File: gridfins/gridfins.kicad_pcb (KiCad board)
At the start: 4 copper layers, 76 parts, among them J1 RBUS, J2 USB_C_Receptacle_USB2.0, U1 ESP32-S3, U2 SN65HVD230, U3 LM66200DRLR, U4 MAX77827AEFD+T, U5 SC4215ASTRT, Y1 R940000171

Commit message: Update with Inertial Measurement Unit
cloned IMU from pickle rick.
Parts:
- added C12: 10uF, Capacitor_SMD:C_0402_1005Metric, F.Cu at (174.7, 55.1)
- added C18: 160pF, Capacitor_SMD:C_0603_1608Metric, F.Cu at (165.3, 29.6)
- added C19: 47uF, Capacitor_SMD:C_1206_3216Metric, F.Cu at (150.6, 22.3)
- added C28: 1uF, Capacitor_SMD:C_0402_1005Metric, F.Cu at (168.4, 36.7)
- added C29: 4.7uF, Capacitor_SMD:C_0402_1005Metric, F.Cu at (168.4, 38.7)
- added C30: 100uF, Capacitor_Tantalum_SMD:CP_EIA-7360-38_Kemet-E, F.Cu at (158.4, 24.4)
- added C31: 47uF, Capacitor_SMD:C_1206_3216Metric, F.Cu at (150.6, 25.7)
- added C32: 100uF, Capacitor_Tantalum_SMD:CP_EIA-7360-38_Kemet-E, F.Cu at (158.4, 32.0)
- added C33: 47uF, Capacitor_SMD:C_1206_3216Metric, F.Cu at (150.6, 29.0)
- added C34: 100nF, Capacitor_SMD:C_0402_1005Metric, F.Cu at (174.7, 57.1)
- added C35: 47uF, Capacitor_SMD:C_1206_3216Metric, F.Cu at (150.6, 32.4)
- added C36: 0.47uF, Capacitor_SMD:C_0402_1005Metric, F.Cu at (174.7, 59.0)
- added C37: 47uF, Capacitor_SMD:C_1206_3216Metric, F.Cu at (150.6, 35.7)
- added C38: 100nF, Capacitor_SMD:C_0402_1005Metric, F.Cu at (168.4, 40.7)
- added C39: 0.1uF, Capacitor_SMD:C_0402_1005Metric, F.Cu at (168.4, 42.6)
- added C40: 47uF, Capacitor_SMD:C_1206_3216Metric, F.Cu at (150.6, 39.1)
- added C41: 10nF, Capacitor_SMD:C_0402_1005Metric, F.Cu at (174.7, 61.0)
- added C42: 0.1uF, Capacitor_SMD:C_0402_1005Metric, F.Cu at (174.7, 63.0)
- added C43: 2.2uF, Capacitor_SMD:C_0402_1005Metric, F.Cu at (174.7, 65.0)
- added C44: 10uF, Capacitor_SMD:C_0402_1005Metric, F.Cu at (174.7, 66.9)
- added C45: 0.1uF, Capacitor_SMD:C_0402_1005Metric, F.Cu at (187.8, 57.1)
- added C46: 47uF, Capacitor_SMD:C_1206_3216Metric, F.Cu at (150.6, 42.4)
- added C47: 47uF, Capacitor_SMD:C_1206_3216Metric, F.Cu at (150.6, 45.8)
- added C48: 47uF, Capacitor_SMD:C_1206_3216Metric, F.Cu at (150.6, 49.1)
- added C49: 47uF, Capacitor_SMD:C_1206_3216Metric, F.Cu at (150.6, 52.5)
- added C50: 1uF, Capacitor_SMD:C_0402_1005Metric, F.Cu at (174.7, 68.9)
- added D3: LED, LED_SMD:LED_0402_1005Metric, F.Cu at (188.1, 55.1)
- added D4: ~, Package_TO_SOT_SMD:SOT-353_SC-70-5, F.Cu at (188.9, 22.7)
- added D5: ~, Package_TO_SOT_SMD:SOT-353_SC-70-5, F.Cu at (188.9, 26.6)
- added D6: ~, Package_TO_SOT_SMD:SOT-353_SC-70-5, F.Cu at (188.9, 30.5)
- added D7: ~, Package_TO_SOT_SMD:SOT-353_SC-70-5, F.Cu at (188.9, 34.4)
- added J3: ServoCH0, iclr:Molex_Nano-Fit_105313-xx03_1x03_P2.50mm_Horizontal, F.Cu at (175.4, 23.4)
- added J4: ServoCH1, iclr:Molex_Nano-Fit_105313-xx03_1x03_P2.50mm_Horizontal, F.Cu at (175.4, 33.9)
- added J5: ServoCH2, iclr:Molex_Nano-Fit_105313-xx03_1x03_P2.50mm_Horizontal, F.Cu at (175.4, 44.4)
- added L4: 3.3uH, iclr:IND_SPM10065VT-3R3M-D, F.Cu at (160.2, 41.5)
- added Q1: SSM3K15AMFV,L3F, iclr:SOT-723, F.Cu at (169.1, 29.8)
- added R19: R, Resistor_SMD:R_0402_1005Metric, F.Cu at (184.9, 55.1)
- added R20: 10k, Resistor_SMD:R_0402_1005Metric, F.Cu at (154.8, 48.3)
- added R21: 113k, Resistor_SMD:R_0402_1005Metric, F.Cu at (154.8, 50.3)
- added R22: 200k, Resistor_SMD:R_0402_1005Metric, F.Cu at (154.8, 52.3)
- added R23: 100k, Resistor_SMD:R_0402_1005Metric, F.Cu at (157.8, 48.3)
- added R24: 442k, Resistor_SMD:R_0402_1005Metric, F.Cu at (157.8, 50.3)
- added R25: 165R, Resistor_SMD:R_0402_1005Metric, F.Cu at (188.2, 37.4)
- added R26: 165R, Resistor_SMD:R_0402_1005Metric, F.Cu at (188.2, 39.3)
- added R27: 165R, Resistor_SMD:R_0402_1005Metric, F.Cu at (188.2, 41.3)
- added R28: 10k, Resistor_SMD:R_0402_1005Metric, F.Cu at (157.8, 52.3)
- added R29: 2.2, Resistor_SMD:R_0402_1005Metric, F.Cu at (160.7, 48.3)
- added R34: 18k, Resistor_SMD:R_0402_1005Metric, F.Cu at (184.9, 57.1)
- added R36: 1.5k, Resistor_SMD:R_0402_1005Metric, F.Cu at (184.9, 59.1)
- added R37: 470, Resistor_SMD:R_0402_1005Metric, F.Cu at (184.9, 61.1)
- added R38: 10k, Resistor_SMD:R_0402_1005Metric, F.Cu at (160.7, 50.3)
- added R39: 1k, Resistor_SMD:R_0402_1005Metric, F.Cu at (160.7, 52.3)
- added R42: 5.1R, Resistor_SMD:R_0603_1608Metric, F.Cu at (165.3, 32.1)
- added TP25: TestPoint, TestPoint:TestPoint_Pad_D1.0mm, F.Cu at (108.9, 89.5)
- added TP26: TestPoint, TestPoint:TestPoint_Pad_D1.0mm, F.Cu at (108.9, 92.6)
- added TP27: TestPoint, TestPoint:TestPoint_Pad_D1.0mm, F.Cu at (108.9, 95.6)
- added U6: SiC437AED-T1, iclr:SiC437BEDT1GE3, F.Cu at (167.3, 24.6)
- added U7: ICM-20608-G, iclr:PQFN50P300X300X80-16N, F.Cu at (179.0, 61.8)
- added U8: MMC5983MA, iclr:PQFN50P300X300X100-16N, F.Cu at (178.8, 66.3)
- added U9: H3LIS331DLTR, iclr:QFN300X300X100-16N, F.Cu at (178.8, 56.8)
- moved C11 75.4 mm to (98.5, 41.2)
- moved C13 75.4 mm to (98.5, 43.2)
- moved C14 75.4 mm to (98.5, 45.1)
- moved D1 75.4 mm to (111.6, 73.4)
- moved J1 75.4 mm to (79.2, 45.2)
- moved JP3 75.4 mm to (92.1, 55.9)
- moved L1 75.4 mm to (92.7, 31.3)
- moved L2 75.4 mm to (92.7, 33.2)
- moved R1 75.4 mm to (92.7, 35.2)
- moved R18 75.4 mm to (95.7, 39.2)
- moved R2 75.4 mm to (92.7, 37.2)
- moved R3 75.4 mm to (92.7, 39.2)
- moved R4 75.4 mm to (95.7, 31.3)
- moved R5 75.4 mm to (95.7, 33.2)
- moved R6 75.4 mm to (95.7, 35.2)
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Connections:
- U1 pad 13: unconnected-(U1-GPIO8/ADC1_CH7-Pad13) -> /HSPI_MISO
- U1 pad 14: unconnected-(U1-GPIO9/ADC1_CH8-Pad14) -> /HSPI_MOSI
- U1 pad 15: unconnected-(U1-GPIO10/ADC1_CH9-Pad15) -> /HSPI_SCLK
- U1 pad 16: unconnected-(U1-GPIO11/ADC2_CH0-Pad16) -> /IMU1_CS
- U1 pad 17: unconnected-(U1-GPIO12/ADC2_CH1-Pad17) -> /IMU2_CS
- U1 pad 18: unconnected-(U1-GPIO13/ADC2_CH2-Pad18) -> /MAG_CS
- U1 pad 39: unconnected-(U1-GPIO34-Pad39) -> /SERVOPWM0
- U1 pad 40: unconnected-(U1-GPIO35-Pad40) -> /SERVOPWM1
- U1 pad 41: unconnected-(U1-GPIO36-Pad41) -> /SERVOPWM2

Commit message: deleted obsolete ICM-20608-G from IMU, added WSEN-ISDS adviced by Jack, a 6 axis IMU. Added footprint and symbol. Yet to finish connections and finish the "application circuit". Added footprint for 6pin connector in Linear Actuator sheet.
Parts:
- added C51: 0.1uF, Capacitor_SMD:C_0402_1005Metric, F.Cu at (143.1, 83.3)
- added C52: 0.1uF, Capacitor_SMD:C_0402_1005Metric, F.Cu at (154.1, 94.0)
- added C53: 1uF, Capacitor_SMD:C_0402_1005Metric, F.Cu at (154.1, 96.0)
- added C54: 0.1uF, Capacitor_SMD:C_0603_1608Metric, F.Cu at (157.6, 99.3)
- added C55: 0.1uF, Capacitor_SMD:C_0402_1005Metric, F.Cu at (154.1, 98.0)
- added J6: ST1W008S4TR2000, iclr:JAE_ST1W008S4TR2000, F.Cu at (139.4, 75.6)
- added J7: Conn_01x06_Pin, Connector_PinHeader_2.54mm:PinHeader_1x06_P2.54mm_Vertical, F.Cu at (152.1, 70.3)
- added JP34: SolderJumper_2_Open, iclr:SmallerSolderJP, F.Cu at (140.2, 83.6)
- added Q3: DMP3099, Package_TO_SOT_SMD:SOT-23, F.Cu at (132.8, 84.5)
- added Q5: BSZ025N04LS, iclr:BSZ025N04LS, F.Cu at (152.3, 89.9)
- added Q6: BSZ025N04LS, iclr:BSZ025N04LS, F.Cu at (157.4, 89.9)
- added R30: 10k, Resistor_SMD:R_0402_1005Metric, F.Cu at (136.7, 83.3)
- added R31: 10k, Resistor_SMD:R_0402_1005Metric, F.Cu at (151.2, 94.0)
- added R32: 100k, Resistor_SMD:R_0402_1005Metric, F.Cu at (151.2, 96.0)
- added R33: 5.1k, Resistor_SMD:R_0402_1005Metric, F.Cu at (151.2, 98.0)
- added R35: 4.22k, Resistor_SMD:R_0402_1005Metric, F.Cu at (151.2, 100.0)
- added R71: 1k, Resistor_SMD:R_0402_1005Metric, F.Cu at (136.7, 85.3)
- added TP3: TestPoint, TestPoint:TestPoint_Pad_D1.0mm, F.Cu at (157.9, 69.5)
- added TP7: TestPoint, TestPoint:TestPoint_Pad_D1.0mm, F.Cu at (157.9, 72.5)
- added U10: LM74810, iclr:SON50P300X300X80-13N-D, F.Cu at (158.2, 95.7)
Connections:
- C30 pad 1: +16.8V -> /VOUTSwitch
- C32 pad 1: +16.8V -> /VOUTSwitch
- C38 pad 1: +16.8V -> /VOUTSwitch
- Q1 pad 1: /Buck/BUCK_EN -> /BUCK_EN
- R38 pad 2: +16.8V -> /VOUTSwitch
- R39 pad 2: /Buck/BUCK_EN -> /BUCK_EN
- U1 pad 10: unconnected-(U1-GPIO5/ADC1_CH4-Pad10) -> /SD1_CS
- U1 pad 11: unconnected-(U1-GPIO6/ADC1_CH5-Pad11) -> /VSPI_MOSI
- U1 pad 12: unconnected-(U1-GPIO7/ADC1_CH6-Pad12) -> /VSPI_SCLK
- U1 pad 13: /HSPI_MISO -> /VSPI_MISO
- U1 pad 14: /HSPI_MOSI -> /HSPI_MISO
- U1 pad 15: /HSPI_SCLK -> /HSPI_MOSI
- U1 pad 16: /IMU1_CS -> /HSPI_SCLK
- U1 pad 17: /IMU2_CS -> /IMU1_CS
- U1 pad 18: /MAG_CS -> /IMU2_CS
- U1 pad 19: unconnected-(U1-GPIO14/ADC2_CH3-Pad19) -> /MAG_CS
- U1 pad 42: unconnected-(U1-GPIO37-Pad42) -> /HSIDE_EN
- U1 pad 43: unconnected-(U1-GPIO38-Pad43) -> /ENCODER_CS
- U1 pad 51: unconnected-(U1-GPIO45-Pad51) -> /BUCK_EN
- U1 pad 6: unconnected-(U1-GPIO1/ADC1_CH0-Pad6) -> /BUS_VMON
- U1 pad 7: unconnected-(U1-GPIO2/ADC1_CH1-Pad7) -> /SD1_DET
- U1 pad 9: unconnected-(U1-GPIO4/ADC1_CH3-Pad9) -> /SD_EN
- U6 pad 1: +16.8V -> /VOUTSwitch
- U6 pad 2: +16.8V -> /VOUTSwitch
- U6 pad 22: +16.8V -> /VOUTSwitch
- U6 pad 26: +16.8V -> /VOUTSwitch

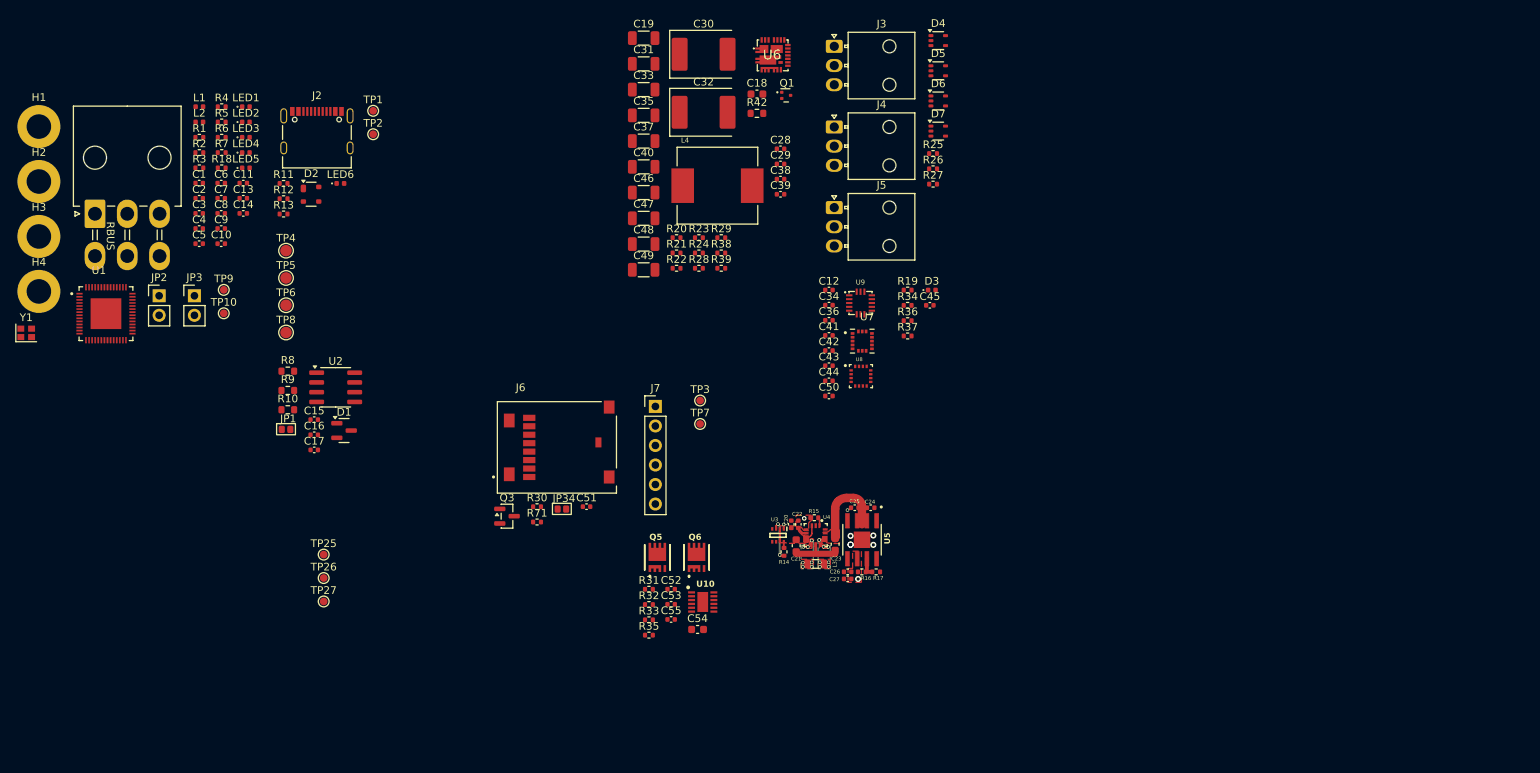
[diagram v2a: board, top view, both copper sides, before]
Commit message: PCB design
Started drawing fill-out zones and organising the recommended PCB layout for the SiC437, 438 on the buck converter
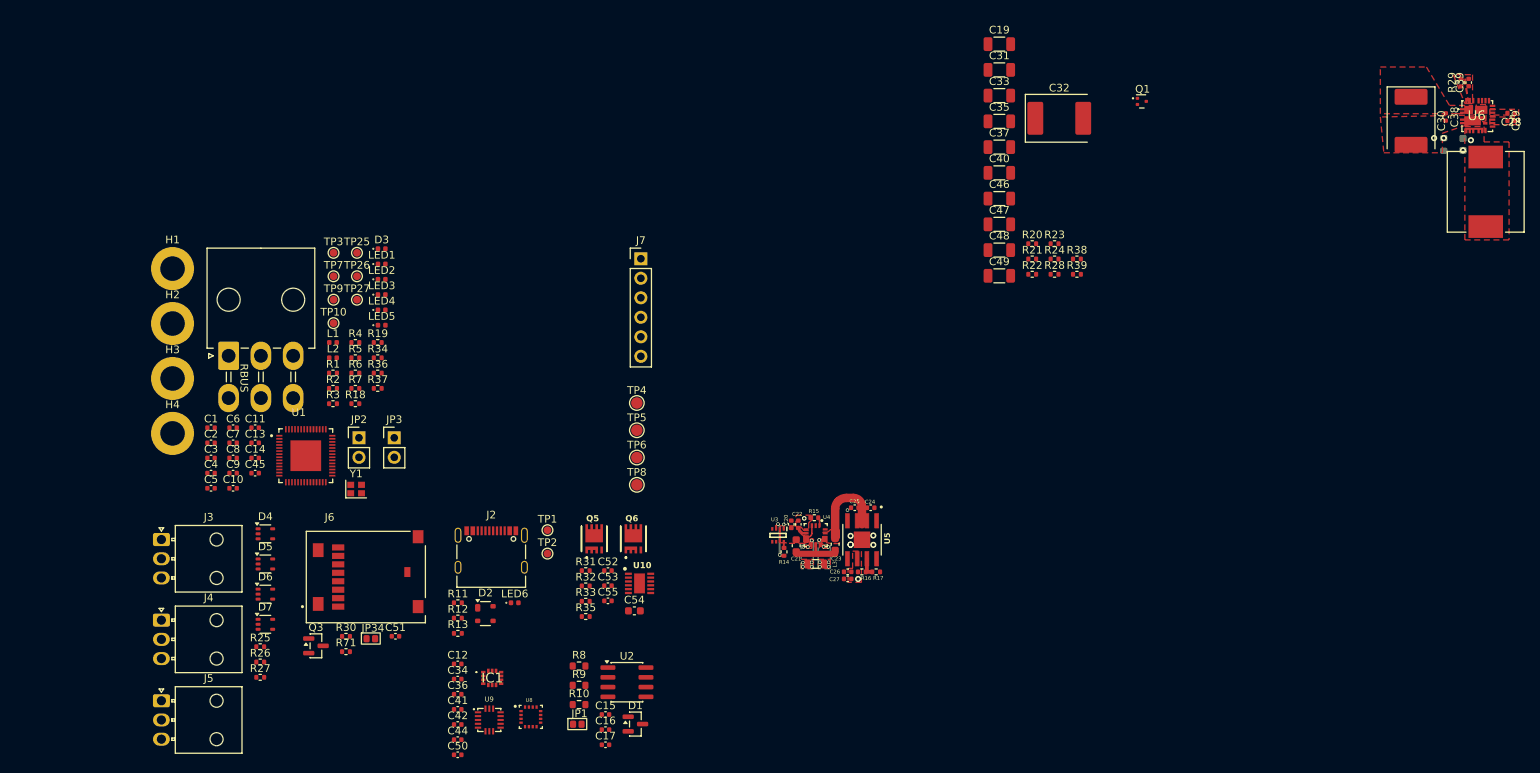
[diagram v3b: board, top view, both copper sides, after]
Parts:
- removed C43: 2.2uF, Capacitor_SMD:C_0402_1005Metric
- removed U7: ICM-20608-G, iclr:PQFN50P300X300X80-16N
- added IC1: 2536030320001, iclr:2536030320001, F.Cu at (130.9, 105.6)
- C18, R42: moved to B.Cu
- C36: value 0.47uF -> 100nF
- C41: value 10nF -> 10uF
- C42: value 0.1uF -> 100nF
- moved D4 108.6 mm to (101.3, 86.8)
- moved D5 108.6 mm to (101.3, 90.8)
- moved D6 108.6 mm to (101.3, 94.7)
- moved D7 108.6 mm to (101.3, 98.6)
- moved J3 108.6 mm to (87.8, 87.6)
- moved J4 108.6 mm to (87.8, 98.1)
- moved J5 108.6 mm to (87.8, 108.6)
- moved R25 108.6 mm to (100.7, 101.5)
- moved R27 108.6 mm to (100.7, 105.5)
- moved R26 108.6 mm to (100.7, 103.5)
- moved L4 100.0 mm to (260.1, 42.3), turned to -90 degrees
- moved R29 98.4 mm to (256.9, 28.1), turned to 90 degrees
- moved C29 95.2 mm to (263.4, 33.1), turned to 180 degrees
- moved C28 95.2 mm to (263.4, 32.1), turned to 180 degrees
- moved C30 92.5 mm to (250.4, 33.1), turned to -90 degrees
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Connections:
- C36 pad 1: Net-(U7-REGOUT) -> +3V3
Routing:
- net GND: vias 8 -> 10
- net /Buck/SW: vias 0 -> 2
- added copper zone on F.Cu, net /Buck/BOOT
- added copper zone on F.Cu, net /Buck/PHASE
- added copper zone on F.Cu, net /Buck/SW
- added copper zone on F.Cu, net /Buck/VDD
- added copper zone on F.Cu, net /VOUTSwitch
- added copper zone on F.Cu, net Net-(U6-V_DRV)

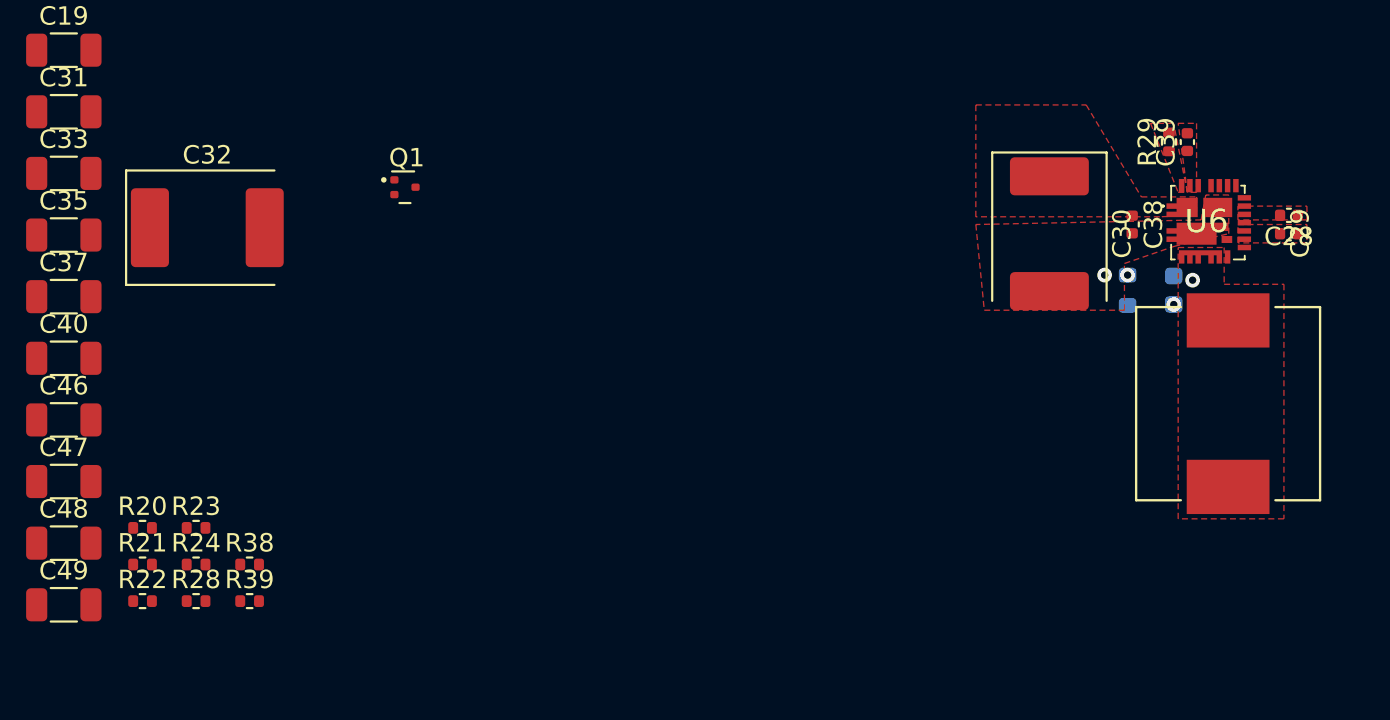
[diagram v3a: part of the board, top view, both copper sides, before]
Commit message: buck PCB
progress - starting from buck converter STEP 4
- Rboot ad Cboot placed near the chip and between pin 23 and 24. Both capcitor and resistor of the recommended size 0402

moved snubber up to top layer

began to move
analog components to left side while power components to right of IC
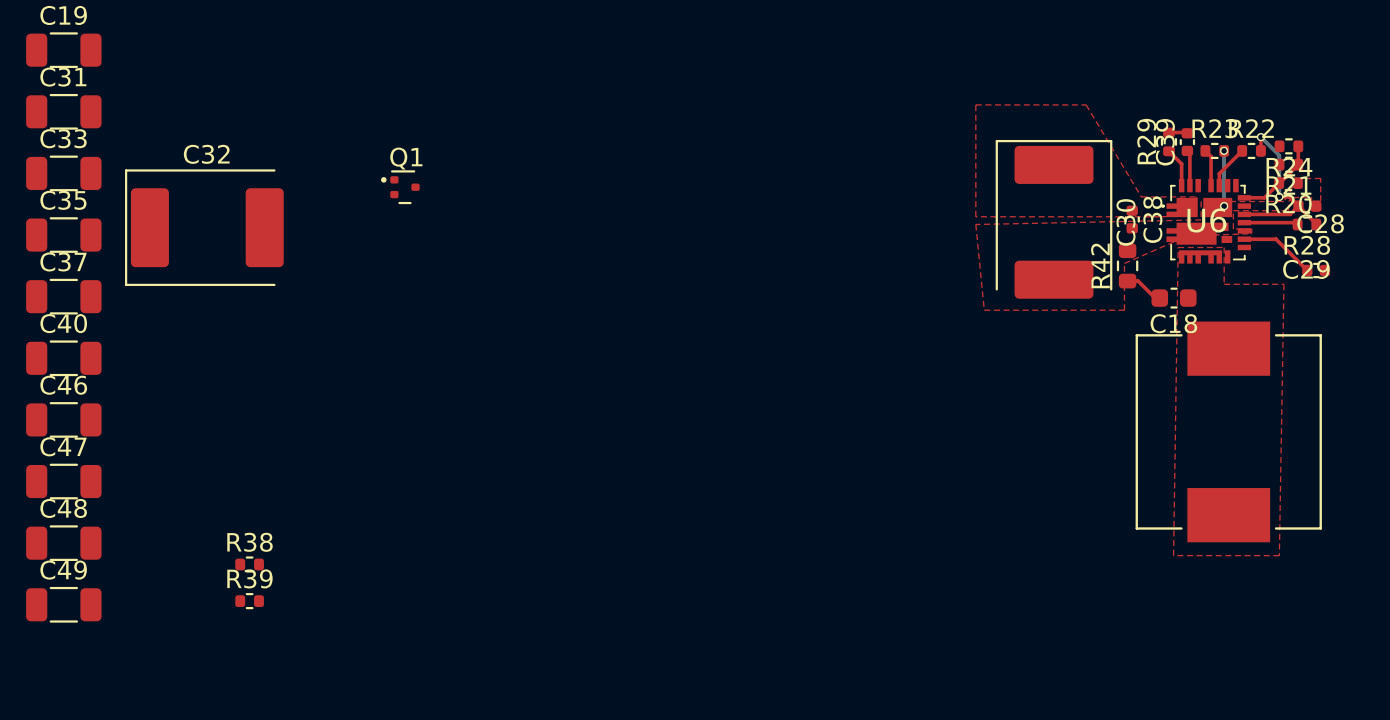
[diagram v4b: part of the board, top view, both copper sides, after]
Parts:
- C18, R42: moved to F.Cu
- moved R21 66.0 mm to (263.4, 29.3), turned to 180 degrees
- moved R22 65.1 mm to (261.4, 28.6)
- moved R20 65.1 mm to (263.4, 30.3), turned to 180 degrees
- moved R28 63.8 mm to (264.4, 32.6), turned to 180 degrees
- moved R24 63.6 mm to (263.4, 28.3), turned to 180 degrees
- moved R23 59.0 mm to (259.4, 28.6)
- moved C29 2.49 mm to (264.9, 35.1)
- moved L4 1.54 mm to (260.2, 43.9), turned to 90 degrees
- moved R42 1.32 mm to (254.7, 34.8)
- moved C28 1.12 mm to (264.4, 31.6)
- moved C30 0.67 mm to (250.7, 32.5)
- moved C18 0.43 mm to (257.2, 36.6), turned to 180 degrees
- moved C38 0.27 mm to (254.9, 32.3)
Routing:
- net /Buck/VDD: track 0.00 -> 10.2 mm, vias 0 -> 2
- net /Buck/FB: track 0.00 -> 4.68 mm
- net Net-(U6-V_DRV): track 0.00 -> 4.12 mm
- net GND: track 7.31 -> 10.3 mm
- net /BuckPGOOD: track 0.00 -> 2.93 mm
- net Net-(U6-MODE_2): track 0.00 -> 2.40 mm
- net /Buck/PHASE: track 0.00 -> 2.15 mm
- net Net-(C18-Pad2): track 0.00 -> 2.13 mm
- net Net-(U6-_MODE_1): track 0.00 -> 2.02 mm
- net /Buck/BOOT: track 0.00 -> 1.95 mm
- net Net-(C39-Pad2): track 0.00 -> 1.02 mm
- net /Buck/SW: vias 2 -> 0
- removed copper zone on F.Cu, net /Buck/BOOT
- removed copper zone on F.Cu, net /Buck/PHASE
- removed copper zone on F.Cu, net /Buck/VDD
- removed copper zone on F.Cu, net Net-(U6-V_DRV)
